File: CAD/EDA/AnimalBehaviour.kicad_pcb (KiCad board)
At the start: 2 copper layers, 105 x 76.5 mm, 27 parts, among them J1 SSR_INPUT, J10 JSolenoid, J11 LED, J12 Cam, J13 Imaging, J14 Ext Supp, J2 SSR OUT, J3 StimCurrentInject, J4 StimIsoIN, J5 StimIsoIN, J6 Imaging, J7 CAM, J8 TONE, J9 TONE, Q1 IRF540N, U1 4N35

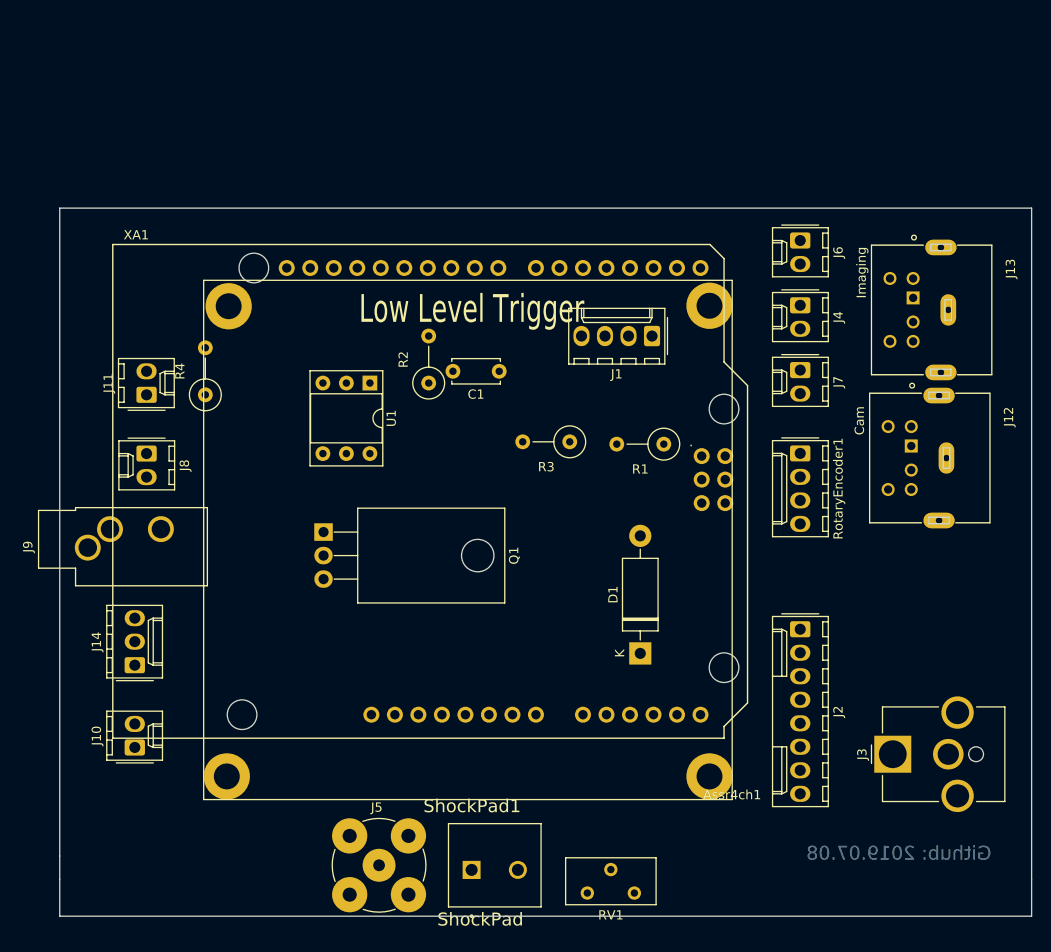
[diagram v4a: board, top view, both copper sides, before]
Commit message: moved C closer to its R.
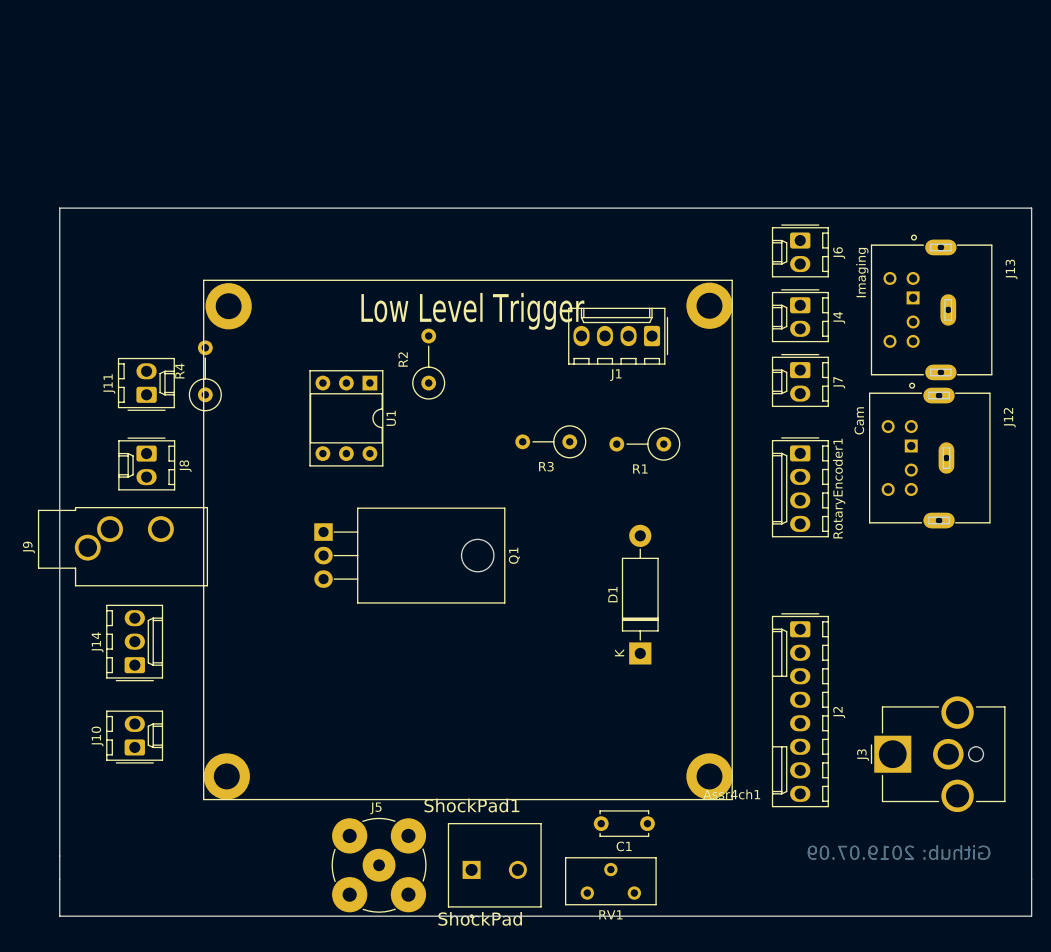
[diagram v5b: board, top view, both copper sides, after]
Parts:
- removed XA1: Arduino_Uno_Shield, Arduino:Arduino_Uno_Shield
- moved C1 51.4 mm to (173.5, 136.5)
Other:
- board text added: "Github: 2019.07.09"
- board text removed: "Github: 2019.07.08"
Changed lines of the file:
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@@
     (tracks 0)
     (zones 0)
-    (modules 27)
+    (modules 26)
     (nets 27)
   )
@@
     (add_net "Net-(D1-Pad2)")
     (add_net "Net-(J11-Pad1)")
-    (add_net "Net-(J12-Pad1)")
-    (add_net "Net-(J12-Pad3)")
-    (add_net "Net-(J12-Pad4)")
-    (add_net "Net-(J12-Pad5)")
-    (add_net "Net-(J13-Pad1)")
-    (add_net "Net-(J13-Pad3)")
-    (add_net "Net-(J13-Pad4)")
-    (add_net "Net-(J13-Pad5)")
     (add_net "Net-(Q1-Pad1)")
     (add_net "Net-(R1-Pad1)")
     (add_net "Net-(R2-Pad1)")
-    (add_net "Net-(RV1-Pad3)")
-    (add_net "Net-(U1-Pad3)")
-    (add_net "Net-(U1-Pad6)")
-    (add_net "Net-(XA1-Pad3V3)")
-    (add_net "Net-(XA1-Pad5V2)")
-    (add_net "Net-(XA1-PadA1)")
-    (add_net "Net-(XA1-PadA2)")
-    (add_net "Net-(XA1-PadA3)")
-    (add_net "Net-(XA1-PadA4)")
-    (add_net "Net-(XA1-PadA5)")
-    (add_net "Net-(XA1-PadAREF)")
-    (add_net "Net-(XA1-PadD0)")
-    (add_net "Net-(XA1-PadD1)")
-    (add_net "Net-(XA1-PadD13)")
-    (add_net "Net-(XA1-PadGND2)")
-    (add_net "Net-(XA1-PadGND3)")
-    (add_net "Net-(XA1-PadGND4)")
-    (add_net "Net-(XA1-PadIORF)")
-    (add_net "Net-(XA1-PadMISO)")
-    (add_net "Net-(XA1-PadMOSI)")
-    (add_net "Net-(XA1-PadRST1)")
-    (add_net "Net-(XA1-PadRST2)")
-    (add_net "Net-(XA1-PadSCK)")
-    (add_net "Net-(XA1-PadSCL)")
-    (add_net "Net-(XA1-PadSDA)")
-    (add_net "Net-(XA1-PadVIN)")
     (add_net OUT+)
     (add_net OUT-)
@@
   )
   (module Capacitor_THT:C_Disc_D5.0mm_W2.5mm_P5.00mm (layer F.Cu)
-    (at 157.48 87.63 180)
+    (at 173.5 136.5 180)
     (descr "C, Disc series, Radial, pin pitch=5.00mm, , diameter*width=5*2.5mm^2, Capacitor, http://cdn-reichelt.de/documents/datenblatt/B300/DS_KERKO_TC.pdf")
     (tags "C Disc series Radial pin pitch 5.00mm  diameter 5mm width 2.5mm Capacitor")
@@
     (pad 1 thru_hole circle (at 26.25 26.9 180) (size 5 5) (drill 2.8) (layers *.Cu *.Mask))
     (pad 1 thru_hole circle (at 26.45 -23.9 180) (size 5 5) (drill 2.8) (layers *.Cu *.Mask))
-  )
-  (module Arduino:Arduino_Uno_Shield (layer F.Cu)
-    (at 115.73 127.27)
-    (descr https://store.arduino.cc/arduino-uno-rev3)
-    (fp_text reference XA1 (at 2.54 -54.356) (layer F.SilkS)
-      (effects (font (size 1 1) (thickness 0.15)))
-    )
-    (fp_text value Arduino_Uno_Shield (at 15.494 -54.356) (layer F.Fab)
-      (effects (font (size 1 1) (thickness 0.15)))
-    )
-    (fp_line (start 0 -53.34) (end 64.516 -53.34) (layer F.SilkS) (width 0.15))
-    (fp_line (start 0 0) (end 66.04 0) (layer F.SilkS) (width 0.15))
-    (fp_line (start 64.516 -53.34) (end 66.04 -51.816) (layer F.SilkS) (width 0.15))
-    (fp_line (start 66.04 0) (end 66.04 -1.27) (layer F.SilkS) (width 0.15))
-    (fp_line (start 66.04 -1.27) (end 68.58 -3.81) (layer F.SilkS) (width 0.15))
-    (fp_line (start 68.58 -3.81) (end 68.58 -38.1) (layer F.SilkS) (width 0.15))
-    (fp_line (start 68.58 -38.1) (end 66.04 -40.64) (layer F.SilkS) (width 0.15))
-    (fp_line (start 66.04 -40.64) (end 66.04 -51.816) (layer F.SilkS) (width 0.15))
-    (fp_line (start 0 -53.34) (end 0 0) (layer F.SilkS) (width 0.15))
-    (fp_line (start -1.905 -12.065) (end 11.43 -12.065) (layer B.CrtYd) (width 0.15))
-    (fp_line (start -1.905 -12.065) (end -1.905 -3.175) (layer B.CrtYd) (width 0.15))
-    (fp_line (start -1.905 -3.175) (end 11.43 -3.175) (layer B.CrtYd) (width 0.15))
-    (fp_line (start 11.43 -12.065) (end 11.43 -3.175) (layer B.CrtYd) (width 0.15))
-    (fp_text user . (at 62.484 -32.004) (layer F.SilkS)
-      (effects (font (size 1 1) (thickness 0.15)))
-    )
-    (fp_line (start -6.35 -43.815) (end -6.35 -32.385) (layer B.CrtYd) (width 0.15))
-    (fp_line (start 9.525 -43.815) (end 9.525 -32.385) (layer B.CrtYd) (width 0.15))
-    (fp_line (start 9.525 -43.815) (end -6.35 -43.815) (layer B.CrtYd) (width 0.15))
-    (fp_line (start 9.525 -32.385) (end -6.35 -32.385) (layer B.CrtYd) (width 0.15))
-    (pad MISO thru_hole oval (at 63.627 -30.48) (size 1.7272 1.7272) (drill 1.016) (layers *.Cu *.Mask))
-    (pad A5 thru_hole oval (at 63.5 -2.54) (size 1.7272 1.7272) (drill 1.016) (layers *.Cu *.Mask))
-    (pad A4 thru_hole oval (at 60.96 -2.54) (size 1.7272 1.7272) (drill 1.016) (layers *.Cu *.Mask))
-    (pad A3 thru_hole oval (at 58.42 -2.54) (size 1.7272 1.7272) (drill 1.016) (layers *.Cu *.Mask))
-    (pad A2 thru_hole oval (at 55.88 -2.54) (size 1.7272 1.7272) (drill 1.016) (layers *.Cu *.Mask))
-    (pad A1 thru_hole oval (at 53.34 -2.54) (size 1.7272 1.7272) (drill 1.016) (layers *.Cu *.Mask))
-    (pad "" thru_hole oval (at 27.94 -2.54) (size 1.7272 1.7272) (drill 1.016) (layers *.Cu *.Mask))
-    (pad D11 thru_hole oval (at 34.036 -50.8) (size 1.7272 1.7272) (drill 1.016) (layers *.Cu *.Mask)
-      (net 17 Puff))
-    (pad D12 thru_hole oval (at 31.496 -50.8) (size 1.7272 1.7272) (drill 1.016) (layers *.Cu *.Mask)
-      (net 14 ImagingTrig))
-    (pad D13 thru_hole oval (at 28.956 -50.8) (size 1.7272 1.7272) (drill 1.016) (layers *.Cu *.Mask))
-    (pad AREF thru_hole oval (at 23.876 -50.8) (size 1.7272 1.7272) (drill 1.016) (layers *.Cu *.Mask))
-    (pad SDA thru_hole oval (at 21.336 -50.8) (size 1.7272 1.7272) (drill 1.016) (layers *.Cu *.Mask))
-    (pad SCL thru_hole oval (at 18.796 -50.8) (size 1.7272 1.7272) (drill 1.016) (layers *.Cu *.Mask))
-    (pad "" np_thru_hole circle (at 13.97 -2.54) (size 3.2 3.2) (drill 3.2) (layers *.Cu *.Mask))
-    (pad "" np_thru_hole circle (at 15.24 -50.8) (size 3.2 3.2) (drill 3.2) (layers *.Cu *.Mask))
-    (pad "" np_thru_hole circle (at 66.04 -35.56) (size 3.2 3.2) (drill 3.2) (layers *.Cu *.Mask))
-    (pad "" np_thru_hole circle (at 66.04 -7.62) (size 3.2 3.2) (drill 3.2) (layers *.Cu *.Mask))
-    (pad D10 thru_hole oval (at 36.576 -50.8) (size 1.7272 1.7272) (drill 1.016) (layers *.Cu *.Mask)
-      (net 15 CamTTL))
-    (pad D9 thru_hole oval (at 39.116 -50.8) (size 1.7272 1.7272) (drill 1.016) (layers *.Cu *.Mask)
-      (net 18 LED))
-    (pad D8 thru_hole oval (at 41.656 -50.8) (size 1.7272 1.7272) (drill 1.016) (layers *.Cu *.Mask)
-      (net 23 TONE+))
-    (pad GND1 thru_hole oval (at 26.416 -50.8) (size 1.7272 1.7272) (drill 1.016) (layers *.Cu *.Mask)
-      (net 24 DGND))
-    (pad D7 thru_hole oval (at 45.72 -50.8) (size 1.7272 1.7272) (drill 1.016) (layers *.Cu *.Mask)
-      (net 13 ShockStimIsolator))
-    (pad D6 thru_hole oval (at 48.26 -50.8) (size 1.7272 1.7272) (drill 1.016) (layers *.Cu *.Mask)
-      (net 21 ShockRelayCh34))
-    (pad D5 thru_hole oval (at 50.8 -50.8) (size 1.7272 1.7272) (drill 1.016) (layers *.Cu *.Mask)
-      (net 12 ShockPWM))
-    (pad D4 thru_hole oval (at 53.34 -50.8) (size 1.7272 1.7272) (drill 1.016) (layers *.Cu *.Mask)
-      (net 22 ShockRelayCh12))
-    (pad D3 thru_hole oval (at 55.88 -50.8) (size 1.7272 1.7272) (drill 1.016) (layers *.Cu *.Mask)
-      (net 19 EncB))
-    (pad D2 thru_hole oval (at 58.42 -50.8) (size 1.7272 1.7272) (drill 1.016) (layers *.Cu *.Mask)
-      (net 20 EncA))
-    (pad D1 thru_hole oval (at 60.96 -50.8) (size 1.7272 1.7272) (drill 1.016) (layers *.Cu *.Mask))
-    (pad D0 thru_hole oval (at 63.5 -50.8) (size 1.7272 1.7272) (drill 1.016) (layers *.Cu *.Mask))
-    (pad IORF thru_hole oval (at 30.48 -2.54) (size 1.7272 1.7272) (drill 1.016) (layers *.Cu *.Mask))
-    (pad RST1 thru_hole oval (at 33.02 -2.54) (size 1.7272 1.7272) (drill 1.016) (layers *.Cu *.Mask))
-    (pad 3V3 thru_hole oval (at 35.56 -2.54) (size 1.7272 1.7272) (drill 1.016) (layers *.Cu *.Mask))
-    (pad 5V1 thru_hole oval (at 38.1 -2.54) (size 1.7272 1.7272) (drill 1.016) (layers *.Cu *.Mask)
-      (net 2 5V))
-    (pad GND2 thru_hole oval (at 40.64 -2.54) (size 1.7272 1.7272) (drill 1.016) (layers *.Cu *.Mask))
-    (pad GND3 thru_hole oval (at 43.18 -2.54) (size 1.7272 1.7272) (drill 1.016) (layers *.Cu *.Mask))
-    (pad VIN thru_hole oval (at 45.72 -2.54) (size 1.7272 1.7272) (drill 1.016) (layers *.Cu *.Mask))
-    (pad A0 thru_hole oval (at 50.8 -2.54) (size 1.7272 1.7272) (drill 1.016) (layers *.Cu *.Mask)
-      (net 11 ShockRead))
-    (pad 5V2 thru_hole oval (at 66.167 -30.48) (size 1.7272 1.7272) (drill 1.016) (layers *.Cu *.Mask))
-    (pad SCK thru_hole oval (at 63.627 -27.94) (size 1.7272 1.7272) (drill 1.016) (layers *.Cu *.Mask))
-    (pad MOSI thru_hole oval (at 66.167 -27.94) (size 1.7272 1.7272) (drill 1.016) (layers *.Cu *.Mask))
-    (pad GND4 thru_hole oval (at 66.167 -25.4) (size 1.7272 1.7272) (drill 1.016) (layers *.Cu *.Mask))
-    (pad RST2 thru_hole oval (at 63.627 -25.4) (size 1.7272 1.7272) (drill 1.016) (layers *.Cu *.Mask))
   )
   (module Diode_THT:D_DO-15_P12.70mm_Horizontal (layer F.Cu)
@@
   (gr_line (start 110 140) (end 110 142.5) (layer Edge.Cuts) (width 0.1))
   (gr_line (start 110 70) (end 110 140) (layer Edge.Cuts) (width 0.1))
-  (gr_text "Github: 2019.07.08" (at 200.66 139.7) (layer B.Cu)
+  (gr_text "Github: 2019.07.09" (at 200.66 139.7) (layer B.Cu)
     (effects (font (size 1.5 1.5) (thickness 0.3)) (justify mirror))
   )

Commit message: version 2019.07.09
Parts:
- added XA1: Arduino_Uno_Shield, Arduino:Arduino_Uno_Shield, F.Cu at (116.0, 126.0)
- moved J6 24.1 mm to (166.5, 68.0), turned to 0 degrees
- moved J4 19.9 mm to (174.5, 68.0), turned to 0 degrees
- moved C1 8.94 mm to (181.5, 140.5), turned to 270 degrees
- moved J3 7.00 mm to (200.0, 122.0)
- moved J7 5.02 mm to (189.5, 82.5)
- moved J13 4.01 mm to (204.5, 77.0)
- moved RV1 1.50 mm to (168.5, 144.0)
- moved J12 1.12 mm to (204.5, 96.0)
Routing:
- net DGND: track 0.00 -> 329.6 mm
- net ShockStimIsolator: track 0.00 -> 170.1 mm
- net CamTTL: track 0.00 -> 144.0 mm
- net ShockPWM: track 0.00 -> 102.0 mm
- net ImagingTrig: track 0.00 -> 94.0 mm
- net Net-(R1-Pad1): track 0.00 -> 78.9 mm
- net 5V: track 0.00 -> 78.9 mm
- net EX_12V: track 0.00 -> 69.3 mm
- net TONE+: track 0.00 -> 68.6 mm
- net Net-(D1-Pad2): track 0.00 -> 66.9 mm
- net Net-(Q1-Pad1): track 0.00 -> 59.7 mm
- net PAD-: track 0.00 -> 57.9 mm
- net AGND: track 0.00 -> 54.9 mm
- net ShockRead: track 0.00 -> 50.3 mm
- net EX_5V: track 0.00 -> 35.6 mm
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- added copper zone on B.Cu, net DGND
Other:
- board size 105 x 76.5 mm -> 106.5 x 83.5 mm

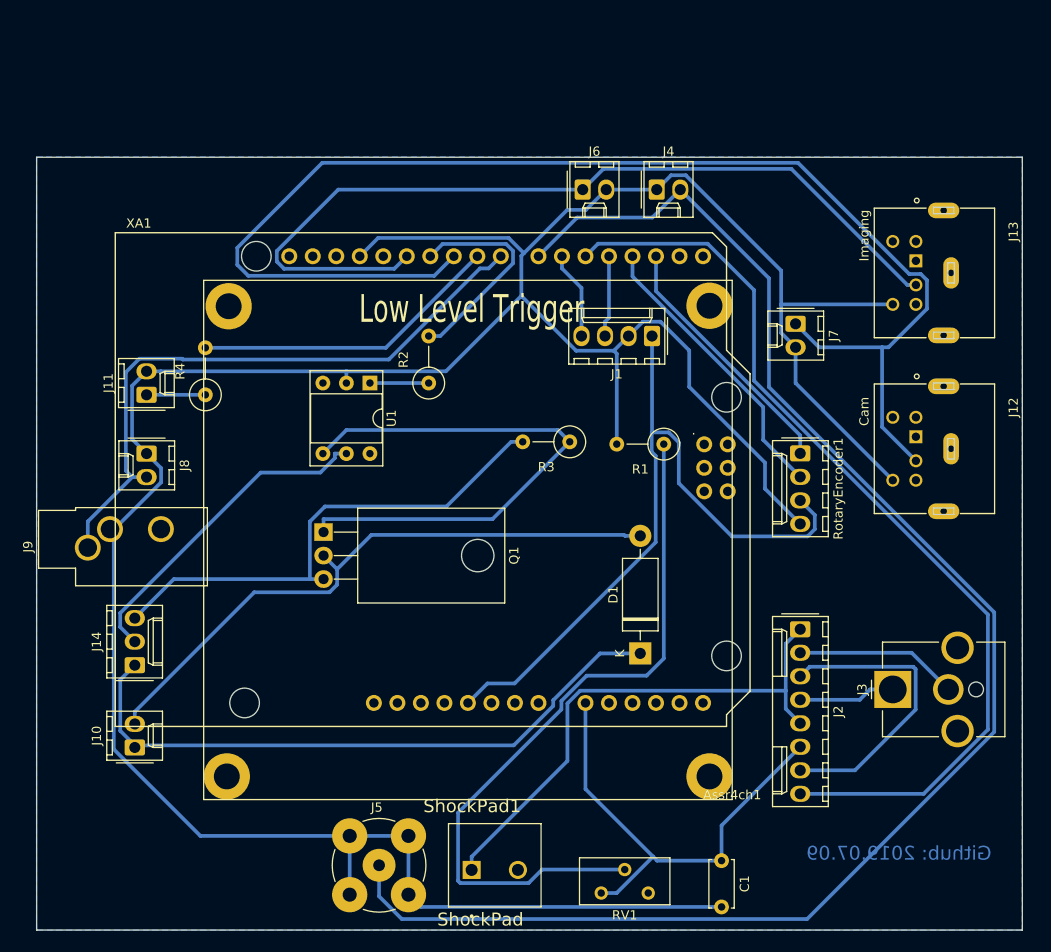
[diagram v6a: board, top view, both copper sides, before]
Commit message: Fixed SHOCKPAD connections. Pins were named 0 and 1. They should have been name 1 and 2.
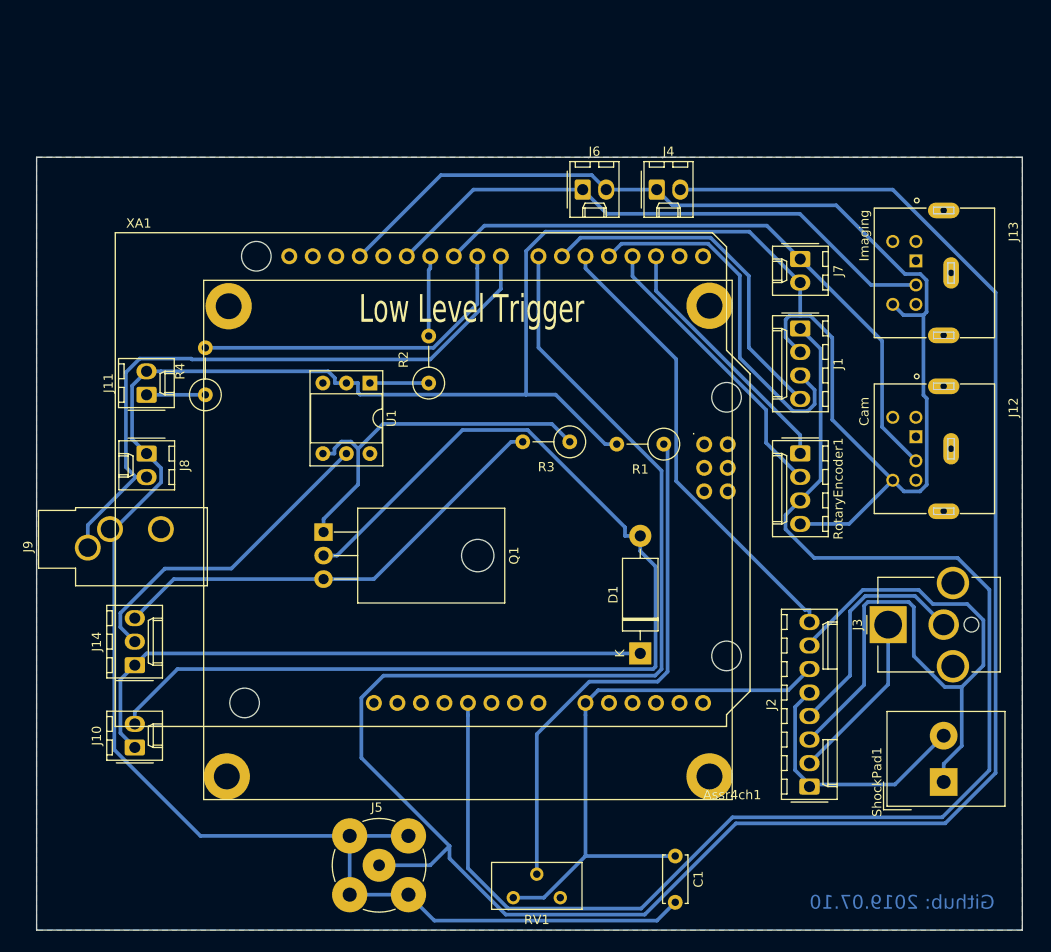
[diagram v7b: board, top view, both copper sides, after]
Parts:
- ShockPad1: footprint BhallaLab:CUI_TB001-500-02BE -> TerminalBlock_Altech:Altech_AK300_1x02_P5.00mm_45-Degree
- moved ShockPad1 51.9 mm to (205.5, 132.0), turned to 90 degrees
- moved J2 17.0 mm to (191.0, 132.5), turned to 90 degrees
- moved J1 16.0 mm to (190.0, 83.0), turned to 270 degrees
- moved RV1 9.51 mm to (159.0, 144.5)
- moved J3 7.02 mm to (199.5, 115.0)
- moved J7 7.02 mm to (190.0, 75.5)
- moved C1 5.02 mm to (176.5, 140.0)
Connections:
- J3 pad 1: OUT+ -> OUT-
- J3 pad 2: OUT- -> OUT+
- ShockPad1 pad 1: PAD- -> PAD+
- ShockPad1 pad 2: (no net) -> PAD-
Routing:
- net ShockStimIsolator: track 170.1 -> 272.0 mm
- net CamTTL: track 144.0 -> 67.3 mm
- net 5V: track 78.9 -> 150.6 mm
- net Net-(D1-Pad2): track 66.9 -> 119.5 mm
- net ShockPWM: track 102.0 -> 49.8 mm
- net PAD+: track 32.6 -> 76.6 mm
- net DGND: track 329.6 -> 372.0 mm
- net ImagingTrig: track 94.0 -> 62.3 mm
- net ShockRelayCh12: track 8.80 -> 39.6 mm
- net PAD-: track 57.9 -> 28.1 mm
- net ShockRelayCh34: track 9.49 -> 38.3 mm
- net Net-(R1-Pad1): track 78.9 -> 56.8 mm
- net Net-(Q1-Pad1): track 59.7 -> 40.3 mm
- net Puff: track 23.5 -> 8.69 mm
- net OUT+: track 10.5 -> 25.2 mm
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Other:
- board text added: "Github: 2019.07.10"
- board text removed: "Github: 2019.07.09"

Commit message: Updated PCB version 2019.08.02
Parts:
- removed C1: 47nF, Capacitor_THT:C_Disc_D5.0mm_W2.5mm_P5.00mm
- removed RV1: R_POT_TRIM, Potentiometer_THT:Potentiometer_Bourns_3296Y_Vertical
- added R1: 10K, Resistor_THT:R_Axial_DIN0309_L9.0mm_D3.2mm_P5.08mm_Vertical, F.Cu at (169.0, 98.5)
- R2: renamed from R1; value 1K -> 100K
- moved R4 34.5 mm to (132.0, 105.0), turned to 270 degrees
- moved R2 9.02 mm to (169.0, 89.0), turned to 90 degrees
- moved R3 2.64 mm to (152.5, 89.0), turned to 0 degrees
- renumbered R2 to R3, R3 to R4, R4 to R5
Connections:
- J2 pad 6: ShockRead -> ShockReadIn
- R2 pad 1: Net-(R1-Pad1) -> ShockRead
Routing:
- net ShockStimIsolator: track 272.0 -> 131.2 mm
- net ShockRelayCh34: track 38.3 -> 154.8 mm
- net CamTTL: track 67.3 -> 146.8 mm
- net PAD+: track 76.6 -> 140.8 mm
- net Net-(R1-Pad1): track 56.8 -> 0.00 mm
- net Net-(D1-Pad2): track 119.5 -> 67.2 mm
- net DGND: track 372.0 -> 406.5 mm
- net ShockReadIn: track 0.00 -> 32.1 mm
- net ImagingTrig: track 62.3 -> 93.9 mm
- net AGND: track 49.8 -> 22.1 mm
- net Net-(Q1-Pad1): track 40.3 -> 15.3 mm
- net 5V: track 150.6 -> 131.4 mm
- net Puff: track 8.69 -> 24.8 mm
- net ShockRead: track 61.6 -> 47.4 mm
- net ShockRelayCh12: track 39.6 -> 26.0 mm
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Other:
- board text added: "Github: 2019.08.02"
- board text removed: "Github: 2019.07.10"
